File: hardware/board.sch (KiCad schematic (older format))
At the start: 37 parts, among them J1 Conn_01x03_Male, J2 Conn_01x03_Male, J3 Conn_01x06, J4 Conn_01x06, J5 Conn_01x06_Female, Q1 AO3400A, Q2 AO3400A, SW1 SW_Push, SW2 SW_Push, U1 HT7850-1-SOT89, U2 HT7833-1-SOT89, U3 ESP32-WROOM-32

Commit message: PCB layout
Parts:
- removed D1: LED, LED_SMD:LED_0805_2012Metric_Pad1.15x1.40mm_HandSolder, symbol Device:LED
- removed D7: LED_RGB, LED_SMD:LED_RGB_5050-6, symbol Device:LED_RGB
- removed R1, R10, R11, R12: 1k, Resistor_SMD:R_0805_2012Metric_Pad1.20x1.40mm_HandSolder, symbol Device:R_Small_US
- J3: footprint Connector_PinHeader_2.54mm:PinHeader_1x06_P2.54mm_Vertical -> Connector_PinHeader_1.00mm:PinHeader_1x06_P1.00mm_Vertical_SMD_Pin1Left
- J4: renamed from J5; footprint Board:Program_Wire -> Board:Wire-Pad-01x06
- J5: renamed from J4; footprint Connector_PinHeader_2.54mm:PinHeader_1x06_P2.54mm_Vertical -> Connector_PinHeader_1.00mm:PinHeader_1x06_P1.00mm_Vertical_SMD_Pin1Left
- renumbered D2 to D1, D3 to D2, D4 to D3, D5 to D4, D6 to D5, R2 to R1, R3 to R2, R4 to R3, R5 to R4, R7 to R5, R8 to R7, R9 to R8
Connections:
- net IO27: now also J5.2 (Pin_2); no longer J5.5 (Pin_5)
- net IO32: no longer names the net of U3.8 (IO32)
- net IO32: no longer J5.4 (Pin_4)
- net IO33: no longer names the net of U3.9 (IO33)
- net IO33: no longer J5.3 (Pin_3)
- net IO34: no longer names the net of U3.6 (IO34)
- net IO34: no longer J5.2 (Pin_2)
- net RGB_B renamed IO26
- net IO26: now also J5.3 (Pin_3)
- net RGB_G renamed IO25
- net IO25: now also J5.4 (Pin_4)
- net RGB_R renamed IO23
- net IO23: now also J5.5 (Pin_5)
- no-connect marks 10 -> 13
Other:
- moved on the sheet: D2, D3, D4, J3, J4, J5, R3, R4, R5, R8, SW1, SW2

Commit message: PCB routed
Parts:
- added D10: LED, LED_SMD:LED_0805_2012Metric_Pad1.15x1.40mm_HandSolder, symbol Device:LED
- added J8: Conn_01x04, Board:Wire-Pad-01x04, symbol Connector_Generic:Conn_01x04
- added R23, R25, R26: 1k, Resistor_SMD:R_0805_2012Metric_Pad1.20x1.40mm_HandSolder, symbol Device:R_Small_US
- added R24: 100R, Resistor_SMD:R_0805_2012Metric_Pad1.20x1.40mm_HandSolder, symbol Device:R_Small_US
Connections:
- net +3V3: now also R23.1
- net GND: now also D10.1 (K), J8.2 (Pin_2)
- net LED_B: now also U3.6 (IO34), R25.2
- net LED_R: now reaches U3.8 (IO32)
- net LED_R: now also R24.2
- net LED_G: now reaches U3.9 (IO33)
- net LED_G: now also R26.2
- new net: D10.2 (A), R23.2
- new net: J8.1 (Pin_1), R24.1
- new net: J8.3 (Pin_3), R26.1
- new net: J8.4 (Pin_4), R25.1
- no-connect marks 13 -> 10
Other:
- moved on the sheet: D2, D3, D4, J3, J4, J5, R3, R4, R5, R8, SW1, SW2

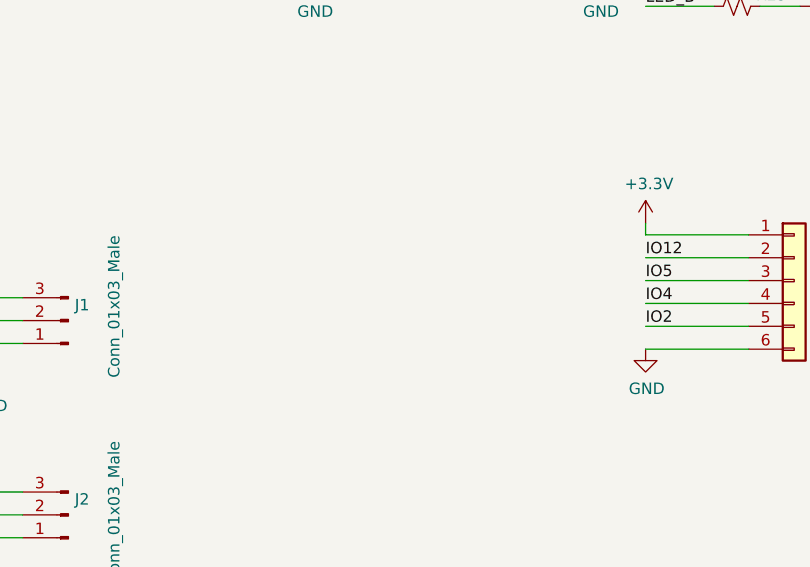
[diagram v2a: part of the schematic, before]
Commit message: PCB: Mounting holes for landing gear
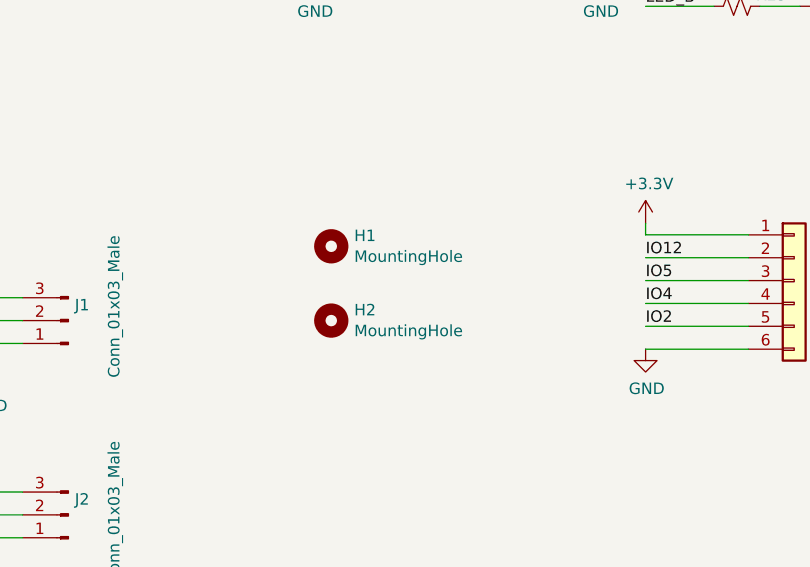
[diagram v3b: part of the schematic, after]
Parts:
- added H1, H2: MountingHole, MountingHole:MountingHole_2.2mm_M2, symbol Mechanical:MountingHole
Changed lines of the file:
@@
+	1    0    0    -1
+$EndComp
+$Comp
+L Mechanical:MountingHole H1
+U 1 1 625E0BE9
+P 6625 5525
+F 0 "H1" H 6725 5571 50  0000 L CNN
+F 1 "MountingHole" H 6725 5480 50  0000 L CNN
+F 2 "MountingHole:MountingHole_2.2mm_M2" H 6625 5525 50  0001 C CNN
+F 3 "~" H 6625 5525 50  0001 C CNN
+	1    6625 5525
+	1    0    0    -1
+$EndComp
+$Comp
+L Mechanical:MountingHole H2
+U 1 1 625E0F52
+P 6625 5850
+F 0 "H2" H 6725 5896 50  0000 L CNN
+F 1 "MountingHole" H 6725 5805 50  0000 L CNN
+F 2 "MountingHole:MountingHole_2.2mm_M2" H 6625 5850 50  0001 C CNN
+F 3 "~" H 6625 5850 50  0001 C CNN
+	1    6625 5850
 	1    0    0    -1
 $EndComp

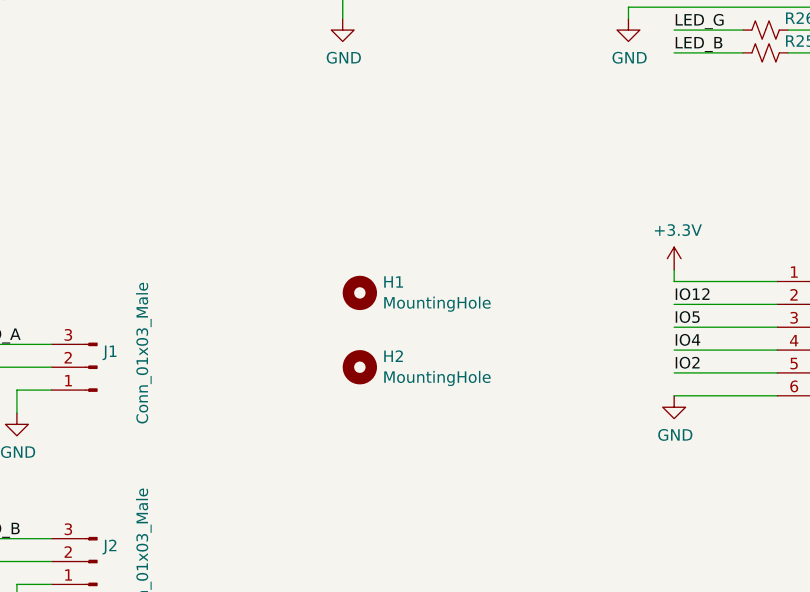
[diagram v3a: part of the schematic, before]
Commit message: PCB: Holes for LiPo battery zip tie added
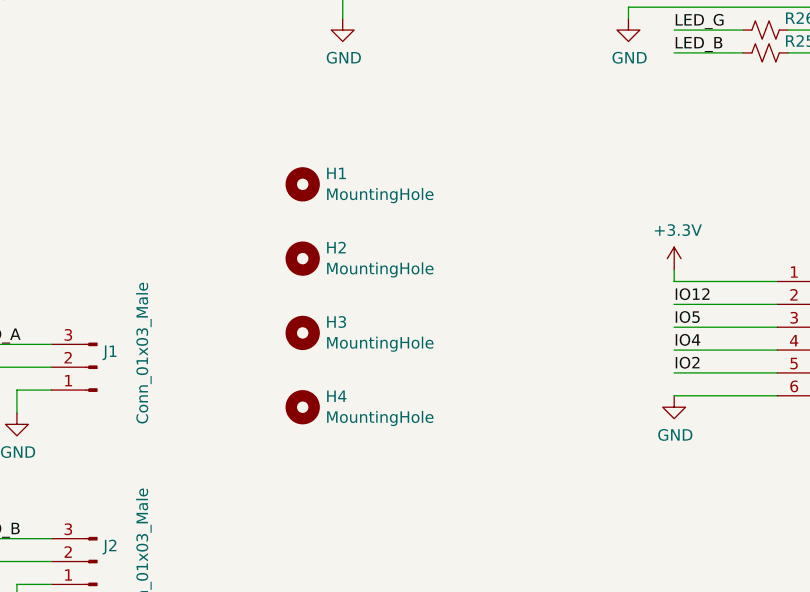
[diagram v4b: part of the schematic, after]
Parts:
- added H3, H4: MountingHole, MountingHole:MountingHole_2.2mm_M2, symbol Mechanical:MountingHole
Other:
- moved on the sheet: H1, H2
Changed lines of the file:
@@
 L Mechanical:MountingHole H1
 U 1 1 625E0BE9
-P 6625 5525
-F 0 "H1" H 6725 5571 50  0000 L CNN
-F 1 "MountingHole" H 6725 5480 50  0000 L CNN
-F 2 "MountingHole:MountingHole_2.2mm_M2" H 6625 5525 50  0001 C CNN
-F 3 "~" H 6625 5525 50  0001 C CNN
-	1    6625 5525
+P 6375 5050
+F 0 "H1" H 6475 5096 50  0000 L CNN
+F 1 "MountingHole" H 6475 5005 50  0000 L CNN
+F 2 "MountingHole:MountingHole_2.2mm_M2" H 6375 5050 50  0001 C CNN
+F 3 "~" H 6375 5050 50  0001 C CNN
+	1    6375 5050
 	1    0    0    -1
 $EndComp
@@
 L Mechanical:MountingHole H2
 U 1 1 625E0F52
-P 6625 5850
-F 0 "H2" H 6725 5896 50  0000 L CNN
-F 1 "MountingHole" H 6725 5805 50  0000 L CNN
-F 2 "MountingHole:MountingHole_2.2mm_M2" H 6625 5850 50  0001 C CNN
-F 3 "~" H 6625 5850 50  0001 C CNN
-	1    6625 5850
+P 6375 5375
+F 0 "H2" H 6475 5421 50  0000 L CNN
+F 1 "MountingHole" H 6475 5330 50  0000 L CNN
+F 2 "MountingHole:MountingHole_2.2mm_M2" H 6375 5375 50  0001 C CNN
+F 3 "~" H 6375 5375 50  0001 C CNN
+	1    6375 5375
 	1    0    0    -1
 $EndComp
+$Comp
+L Mechanical:MountingHole H3
+U 1 1 626D265C
+P 6375 5700
+F 0 "H3" H 6475 5746 50  0000 L CNN
+F 1 "MountingHole" H 6475 5655 50  0000 L CNN
+F 2 "MountingHole:MountingHole_2.2mm_M2" H 6375 5700 50  0001 C CNN
+F 3 "~" H 6375 5700 50  0001 C CNN
+	1    6375 5700
+	1    0    0    -1
+$EndComp
+$Comp
+L Mechanical:MountingHole H4
+U 1 1 626D2662
+P 6375 6025
+F 0 "H4" H 6475 6071 50  0000 L CNN
+F 1 "MountingHole" H 6475 5980 50  0000 L CNN
+F 2 "MountingHole:MountingHole_2.2mm_M2" H 6375 6025 50  0001 C CNN
+F 3 "~" H 6375 6025 50  0001 C CNN
+	1    6375 6025
+	1    0    0    -1
+$EndComp
